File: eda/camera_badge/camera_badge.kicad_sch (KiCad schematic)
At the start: 2 parts, among them U1 ESP32-WROOM-32-DEVKIT

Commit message: badge eda updates
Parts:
- DS1: footprint 0_local:GC9A01_TFT -> 0_local:GC9A01_TFT_Back_Mount
- U1: footprint 0_local:ESP32_DEVKIT_V1 -> 0_local:ESP32_DEVKIT_V1_Back_Mount
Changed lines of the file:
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@@
       (effects (font (size 1.27 1.27)) (justify left))
     )
-    (property "Footprint" "0_local:GC9A01_TFT" (at 167.132 62.6607 0)
+    (property "Footprint" "0_local:GC9A01_TFT_Back_Mount" (at 167.132 62.6607 0)
       (effects (font (size 1.27 1.27)) (justify left))
     )
@@
       (effects (font (size 1.27 1.27)))
     )
-    (property "Footprint" "0_local:ESP32_DEVKIT_V1" (at 70.231 104.775 0)
+    (property "Footprint" "0_local:ESP32_DEVKIT_V1_Back_Mount" (at 70.231 104.775 0)
       (effects (font (size 1.27 1.27)))
     )

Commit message: footprint and schem updates
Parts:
- removed U1: ESP32-WROOM-32-DEVKIT, 0_local:ESP32_DEVKIT_V1_Back_Mount, symbol 0_local:ESP32-WROOM-32-DEVKIT
- added BT1: Battery_Lipo, 0_local:Battery_Connector_back, symbol 0_local:Battery_Lipo
- added D1: LED_WS2812D_THT_5mm, 0_local:LED_D5.0mm-4_WS2812D_2024_back, symbol 0_local:LED_WS2812D_THT_5mm
- added J1: Battery_Conn, 0_local:Battery_Connector_back, symbol 0_local:Battery_Conn
- added SW1: SW_SPDT_SS12D00G, 0_local:SW_SPDT_Slide_SS12D00G-1P2T_3pin_back, symbol 0_local:SW_SPDT_SS12D00G
- added U1: ESP32-WEMOS-LOLIN32-LITE, 0_local:ESP32_WEMOS_LOLIN32_LITE_back, symbol 0_local:ESP32-WEMOS-LOLIN32-LITE
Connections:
- net +3.3V: now also U1.3V3 (3v3)
- net D16: now also U1.16 (GPIO16)
- net D18: now also U1.18 (GPIO18)
- net D23: now also U1.23 (GPIO23)
- net D4: now also U1.4 (GPIO4/TCH0)
- net D5: now also U1.5 (GPIO5)
- net GND: now also U1.GND
- new net: BT1.1 (Pin_1), SW1.2 (B)
- new net GBAT: BT1.2 (Pin_2), J1.2 (Pin_2)
- new net VBAT: J1.1 (Pin_1), SW1.1 (A)
- no-connect marks 0 -> 1
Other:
- note added: "VBAT & GBAT + -"
- note added: "WARNING: JST-PH connector wired reverse polarity from many cables Black wire may go to + & red to - DOUBLE CHECK BEFORE CONNECTING!"
- moved on the sheet: DS1

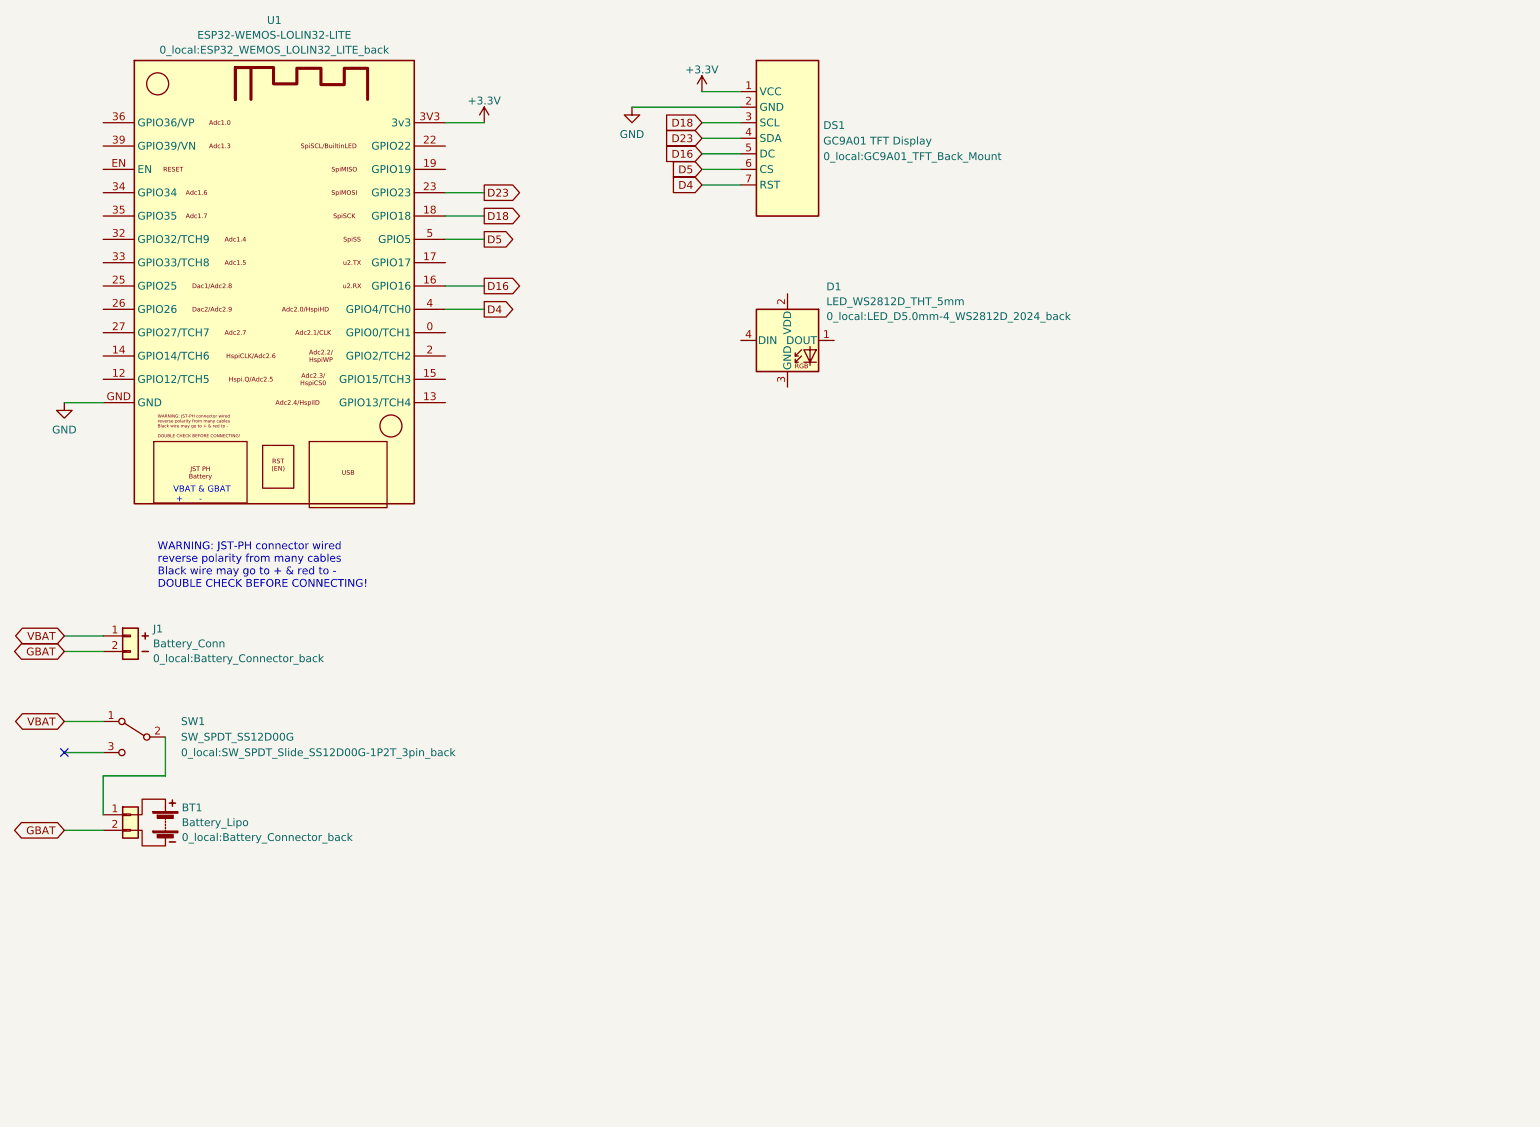
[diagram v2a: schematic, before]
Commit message: footprint and schematic updates
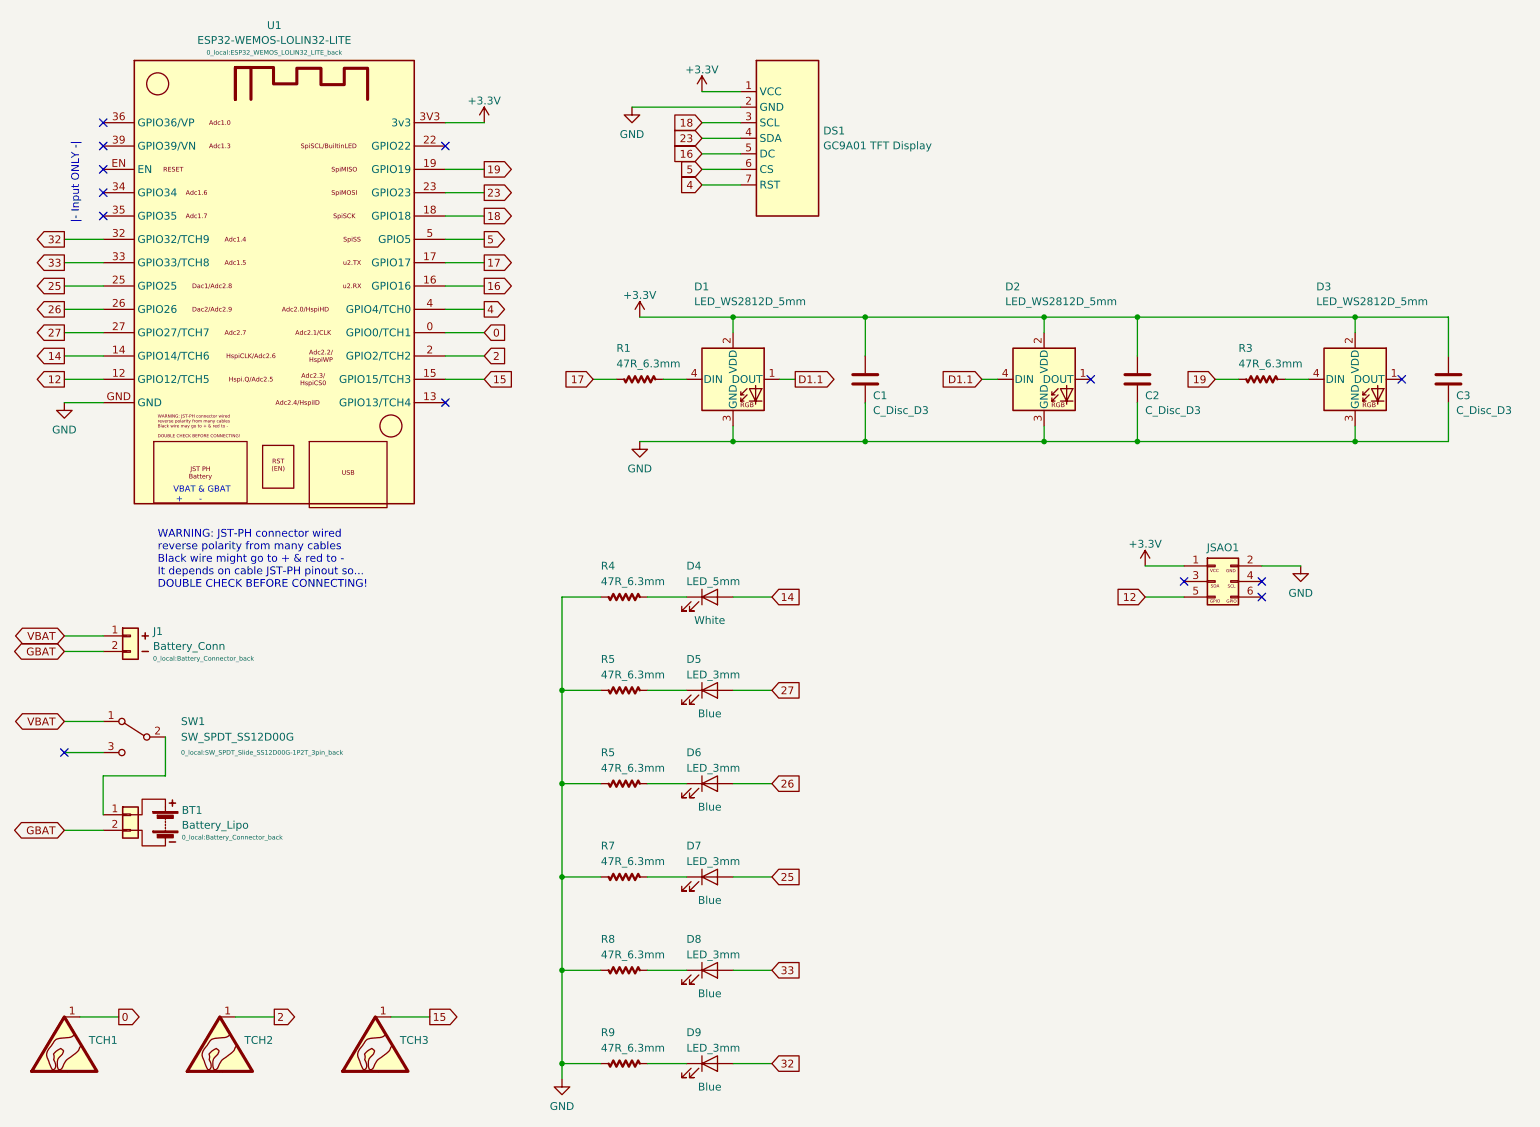
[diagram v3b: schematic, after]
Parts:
- added C1, C2, C3: C_Disc_D3, 0_local:C_Disc_D3_back, symbol 0_local:C_Disc_D3
- added D2, D3: LED_WS2812D_5mm, 0_local:LED_D5.0mm-4_WS2812D_2024_back, symbol 0_local:LED_WS2812D_THT_5mm
- added D4: LED_5mm, 0_local:LED_D5.0mm-2_back, symbol 0_local:LED_THT_5mm
- added D5, D6, D7, D8, D9: LED_3mm, 0_local:LED_D3.0mm-2-std_back, symbol 0_local:LED_THT_3mm
- added JSAO1: Conn_02x03_SAO, 0_sao_v169bis:SAOv169-BADGEv2-2x3_gpio_back, symbol 0_local:Conn_02x03_SAO
- added R1, R3, R4, R5 (x2), R7, R8, R9: 47R_6.3mm, 0_local:R_Axial_DIN0207_L6.3_D2.5_P7.62_Horiz_back, symbol 0_local:R_Axial_Z_L6.3
- added TCH1, TCH2, TCH3: SYM_Touch_lg, symbol 0_local:SYM_Touch_lg
- D1: value LED_WS2812D_THT_5mm -> LED_WS2812D_5mm
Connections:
- net +3.3V: now also D1.2 (VDD), C1.1, C2.1, C3.1, D2.2 (VDD), D3.2 (VDD), JSAO1.1 (Pin_1)
- net GND: now also D1.3 (GND), C1.2, C2.2, C3.2, D2.3 (GND), D3.3 (GND), JSAO1.2 (Pin_2), R4.2, R5.2, R5.2, R7.2, R8.2, R9.2
- net D1.1: now reaches D1.1 (DOUT)
- net D1.1: now also D2.4 (DIN)
- net at D1.4 (DIN): now also R1.1
- net 0: now reaches U1.0 (GPIO0/TCH1)
- net 0: now also TCH1.1
- net 12: now reaches U1.12 (GPIO12/TCH5)
- net 12: now also JSAO1.5 (Pin_5)
- net 14: now reaches U1.14 (GPIO14/TCH6)
- net 14: now also D4.2 (A)
- net 15: now reaches U1.15 (GPIO15/TCH3)
- net 15: now also TCH3.1
- net 17: now reaches U1.17 (GPIO17)
- net 17: now also R1.2
- net 19: now reaches U1.19 (GPIO19)
- net 19: now also R3.2
- net 2: now reaches U1.2 (GPIO2/TCH2)
- net 2: now also TCH2.1
- net 25: now reaches U1.25 (GPIO25)
- net 25: now also D7.2 (A)
- net 26: now reaches U1.26 (GPIO26)
- net 26: now also D6.2 (A)
- net 27: now reaches U1.27 (GPIO27/TCH7)
- net 27: now also D5.2 (A)
- net 32: now reaches U1.32 (GPIO32/TCH9)
- net 32: now also D9.2 (A)
- net 33: now reaches U1.33 (GPIO33/TCH8)
- net 33: now also D8.2 (A)
- net D16 renamed 16
- net D18 renamed 18
- net D23 renamed 23
- net D4 renamed 4
- net D5 renamed 5
- new net: D9.1 (K), R9.1
- new net: D6.1 (K), R5.1
- new net: D4.1 (K), R4.1
- new net: D8.1 (K), R8.1
- new net: D3.4 (DIN), R3.1
- new net: D7.1 (K), R7.1
- new net: D5.1 (K), R5.1
- no-connect marks 1 -> 13
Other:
- note added: "WARNING: JST-PH connector wired reverse polarity from many cables Black wire might go to + & red to - It depends on cable JST-PH pinout so... DOUBLE CHECK BEFORE CONNECTING!"
- note added: "|- Input ONLY -|"
- note removed: "WARNING: JST-PH connector wired reverse polarity from many cables Black wire may go to + & red to - DOUBLE CHECK BEFORE CONNECTING!"
- company: (none) -> Crafted by @alt_bier a.k.a. Richard Gowen and others from Blue Team Village
- title: (none) -> Camera_Badge
- moved on the sheet: D1

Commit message: schematic update
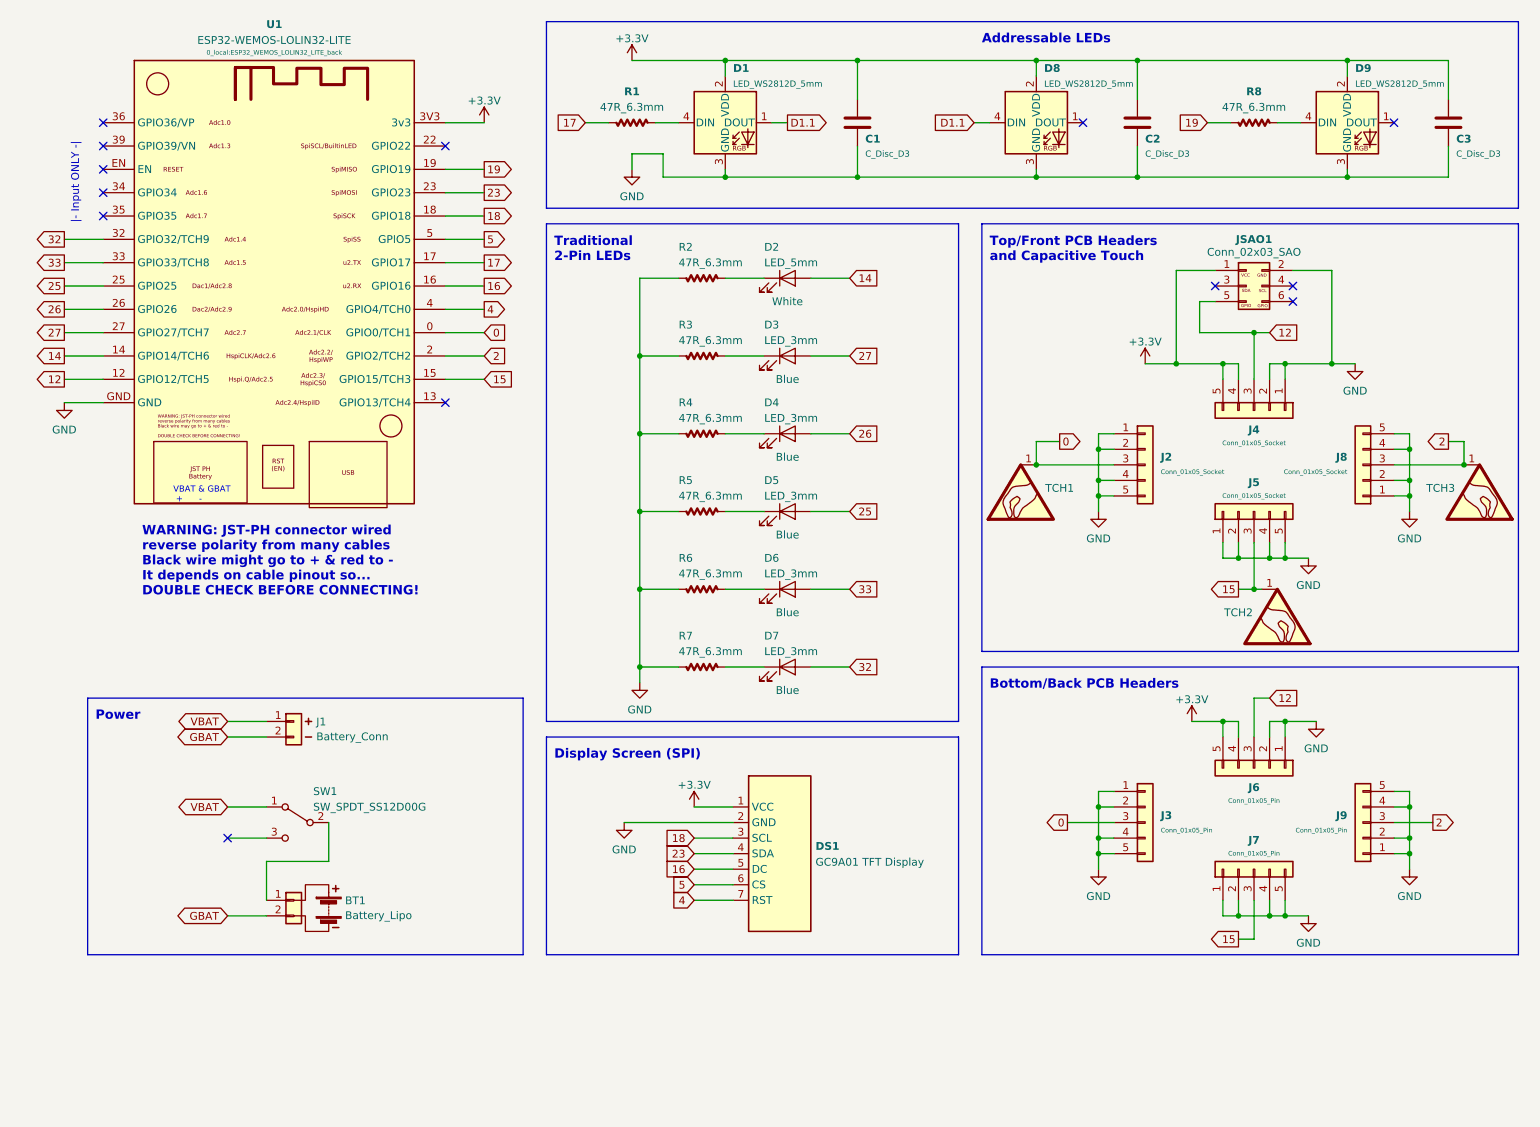
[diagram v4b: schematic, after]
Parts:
- added J2, J4, J5, J8: Conn_01x05_Socket, 0_local:Conn_Pin_Header_Female_Vert_Back_1x05_Pitch2.54mm, symbol 0_local:Conn_01x05_Socket
- added J3, J6, J7, J9: Conn_01x05_Pin, 0_local:Conn_Pin_Header_Male_Vert_Front_1x05_Pitch2.54mm, symbol 0_local:Conn_01x05_Pin
- DS1: footprint 0_local:GC9A01_TFT_Back_Mount -> 0_local:GC9A01_TFT
- renumbered D4 to D2, D5 to D3, D6 to D4, D7 to D5, D8 to D6, D9 to D7, D2 to D8, D3 to D9, R4 to R2, R5 to R3, R5 to R4, R7 to R5, R8 to R6, R9 to R7, R3 to R8, TCH3 to TCH2, TCH2 to TCH3
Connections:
- net +3.3V: now also J4.4 (Pin_4), J4.5 (Pin_5), J6.4 (Pin_4), J6.5 (Pin_5)
- net 0: now also J2.3 (Pin_3), J3.3 (Pin_3)
- net 12: now also J4.3 (Pin_3), J6.3 (Pin_3)
- net 15: now also J5.3 (Pin_3), J7.3 (Pin_3)
- net 2: now also J8.3 (Pin_3), J9.3 (Pin_3)
- net GND: now also J2.1 (Pin_1), J2.2 (Pin_2), J2.4 (Pin_4), J2.5 (Pin_5), J3.1 (Pin_1), J3.2 (Pin_2), J3.4 (Pin_4), J3.5 (Pin_5), J4.1 (Pin_1), J4.2 (Pin_2), J5.1 (Pin_1), J5.2 (Pin_2), J5.4 (Pin_4), J5.5 (Pin_5), J6.1 (Pin_1), J6.2 (Pin_2), J7.1 (Pin_1), J7.2 (Pin_2), J7.4 (Pin_4), J7.5 (Pin_5), J8.1 (Pin_1), J8.2 (Pin_2), J8.4 (Pin_4), J8.5 (Pin_5), J9.1 (Pin_1), J9.2 (Pin_2), J9.4 (Pin_4), J9.5 (Pin_5)
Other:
- note added: "Addressable LEDs"
- note added: "Bottom/Back PCB Headers"
- note added: "Display Screen (SPI)"
- note added: "Power"
- note added: "Top/Front PCB Headers and Capacitive Touch"
- note added: "Traditional 2-Pin LEDs"
- note added: "WARNING: JST-PH connector wired reverse polarity from many cables Black wire might go to + & red to - It depends on cable pinout so... DOUBLE CHECK BEFORE CONNECTING!"
- note removed: "WARNING: JST-PH connector wired reverse polarity from many cables Black wire might go to + & red to - It depends on cable JST-PH pinout so... DOUBLE CHECK BEFORE CONNECTING!"
- moved on the sheet: BT1, C1, C2, C3, D1, D2, D3, D4, D5, D6, D7, D8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

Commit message: pcb work
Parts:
- DS1: footprint 0_local:GC9A01_TFT -> 0_local:GC9A01_TFT_Back_Mount
- J3, J7, J9: footprint 0_local:Conn_Pin_Header_Male_Vert_Front_1x05_Pitch2.54mm -> 0_local:Conn_Pin_Header_Male_Vert_Back_1x05_Pitch2.54mm
- J5: renamed from J6; footprint 0_local:Conn_Pin_Header_Male_Vert_Front_1x05_Pitch2.54mm -> 0_local:Conn_Pin_Header_Male_Vert_Back_1x05_Pitch2.54mm
- renumbered C1 to C10, C2 to C11, C3 to C20, D1 to D10, D8 to D11, D9 to D20, J5 to J6, R1 to R10, R8 to R20

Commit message: pcb trace work
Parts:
- renumbered TCH2 to TCH3, TCH3 to TCH5
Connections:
- net 12: now also J8.3 (Pin_3), J9.3 (Pin_3), TCH5.1; no longer J4.3 (Pin_3), J5.3 (Pin_3), JSAO1.5 (Pin_5)
- net 14: now also D7.2 (A); no longer D2.2 (A)
- net 2: now also J4.3 (Pin_3), J5.3 (Pin_3), JSAO1.5 (Pin_5); no longer J8.3 (Pin_3), J9.3 (Pin_3), TCH5.1
- net 25: now also D6.2 (A); no longer D5.2 (A)
- net 32: now also D2.2 (A); no longer D7.2 (A)
- net 33: now also D5.2 (A); no longer D6.2 (A)

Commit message: pcb updates
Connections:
- net +3.3V: no longer J4.4 (Pin_4), J4.5 (Pin_5), JSAO1.1 (Pin_1)
- net 0: no longer J2.3 (Pin_3), TCH1.1
- net 12: no longer J8.3 (Pin_3), TCH5.1
- net 15: no longer J6.3 (Pin_3), TCH3.1
- net 2: no longer J4.3 (Pin_3), JSAO1.5 (Pin_5)
- net GND: no longer J2.1 (Pin_1), J2.2 (Pin_2), J2.4 (Pin_4), J2.5 (Pin_5), J4.1 (Pin_1), J4.2 (Pin_2), J6.1 (Pin_1), J6.2 (Pin_2), J6.4 (Pin_4), J6.5 (Pin_5), J8.1 (Pin_1), J8.2 (Pin_2), J8.4 (Pin_4), J8.5 (Pin_5), JSAO1.2 (Pin_2)
- new net F0: J2.3 (Pin_3), TCH1.1
- new net F12: J8.3 (Pin_3), TCH5.1
- new net F15: J6.3 (Pin_3), TCH3.1
- new net F2: J4.3 (Pin_3), JSAO1.5 (Pin_5)
- new net GNDFILL: J2.1 (Pin_1), J2.2 (Pin_2), J2.4 (Pin_4), J2.5 (Pin_5), J4.1 (Pin_1), J4.2 (Pin_2), J6.1 (Pin_1), J6.2 (Pin_2), J6.4 (Pin_4), J6.5 (Pin_5), J8.1 (Pin_1), J8.2 (Pin_2), J8.4 (Pin_4), J8.5 (Pin_5), JSAO1.2 (Pin_2)
- new net SAO+3.3V: J4.4 (Pin_4), J4.5 (Pin_5), JSAO1.1 (Pin_1)

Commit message: pcb rev2 updates
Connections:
- net 13: now reaches U1.13 (GPIO13/TCH4)
- net 13: now also J3.3 (Pin_3)
- net 0: no longer names the net of U1.0 (GPIO0/TCH1)
- net 0: no longer J3.3 (Pin_3)
- net F0 renamed F13
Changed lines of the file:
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@@
   (title_block
     (title "Camera_Badge")
-    (date "2024-03-26")
-    (rev "1")
+    (date "2024-04-12")
+    (rev "2")
     (company "Crafted by @alt_bier a.k.a. Richard Gowen and others from Blue Team Village")
   )
@@
   (no_connect (at 33.02 36.83))
   (no_connect (at 88.9 36.83))
-  (no_connect (at 88.9 78.74))
   (no_connect (at 53.34 149.86))
   (no_connect (at 243.84 33.02))
@@
   (no_connect (at 227.33 62.23))
   (no_connect (at 214.63 59.69))
+  (no_connect (at 88.9 67.31))
   (no_connect (at 33.02 40.64))
   (no_connect (at 33.02 33.02))
@@
     (stroke (width 0) (type default))
   )
-  (wire (pts (xy 88.9 67.31) (xy 95.25 67.31))
-    (stroke (width 0) (type default))
-  )
   (wire (pts (xy 88.9 63.5) (xy 95.25 63.5))
     (stroke (width 0) (type default))
@@
   )
   (wire (pts (xy 246.38 144.78) (xy 246.38 149.86))
+    (stroke (width 0) (type default))
+  )
+  (wire (pts (xy 88.9 78.74) (xy 95.25 78.74))
     (stroke (width 0) (type default))
   )
@@
     )
   )
-  (global_label "0" (shape output) (at 190.5 147.32 180) (fields_autoplaced)
-    (effects (font (size 1.27 1.27)) (justify right))
-    (property "Intersheetrefs" "${INTERSHEET_REFS}" (at 186.3053 147.32 0)
+  (global_label "13" (shape output) (at 190.5 147.32 180) (fields_autoplaced)
+    (effects (font (size 1.27 1.27)) (justify right))
+    (property "Intersheetrefs" "${INTERSHEET_REFS}" (at 185.0958 147.32 0)
       (effects (font (size 1.27 1.27)) (justify right) hide)
     )
@@
     )
   )
-  (global_label "0" (shape input) (at 95.25 67.31 0) (fields_autoplaced)
-    (effects (font (size 1.27 1.27)) (justify left))
-    (property "Intersheetrefs" "${INTERSHEET_REFS}" (at 99.4447 67.31 0)
-      (effects (font (size 1.27 1.27)) (justify left) hide)
-    )
-  )
   (global_label "14" (shape input) (at 154.94 121.92 0) (fields_autoplaced)
     (effects (font (size 1.27 1.27)) (justify left))
@@
     )
   )
-  (global_label "F0" (shape output) (at 189.23 85.09 0) (fields_autoplaced)
-    (effects (font (size 1.27 1.27)) (justify left))
-    (property "Intersheetrefs" "${INTERSHEET_REFS}" (at 194.5133 85.09 0)
-      (effects (font (size 1.27 1.27)) (justify left) hide)
-    )
+  (global_label "F13" (shape output) (at 189.23 85.09 0) (fields_autoplaced)
+    (effects (font (size 1.27 1.27)) (justify left))
+    (property "Intersheetrefs" "${INTERSHEET_REFS}" (at 195.7228 85.09 0)
+      (effects (font (size 1.27 1.27)) (justify left) hide)
+    )
+  )
+  (global_label "13" (shape input) (at 95.25 78.74 0) (fields_autoplaced)
+    (effects (font (size 1.27 1.27)) (justify left))
+    (property "Intersheetrefs" "${INTERSHEET_REFS}" (at 100.6542 78.74 0)
+      (effects (font (size 1.27 1.27)) (justify left) hide)
+    )
